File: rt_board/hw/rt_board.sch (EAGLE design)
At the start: 23 parts, among them IC1 MCP170333MB, IC2 FT232RL, Q1 8MHz, U1 STM32F051R8T7, X1 PWR, X2 MINI-USB

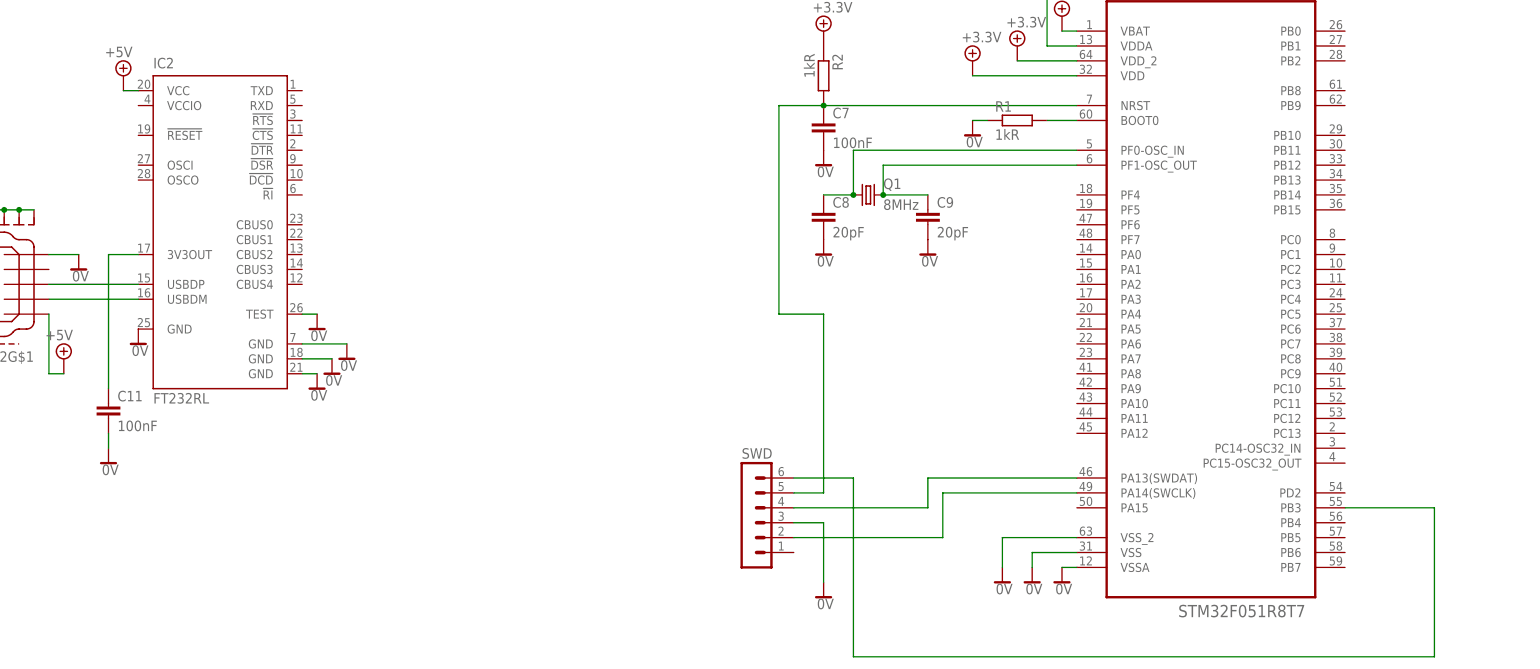
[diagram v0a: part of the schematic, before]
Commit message: fixed SWD connection; added power VccIo to FT232
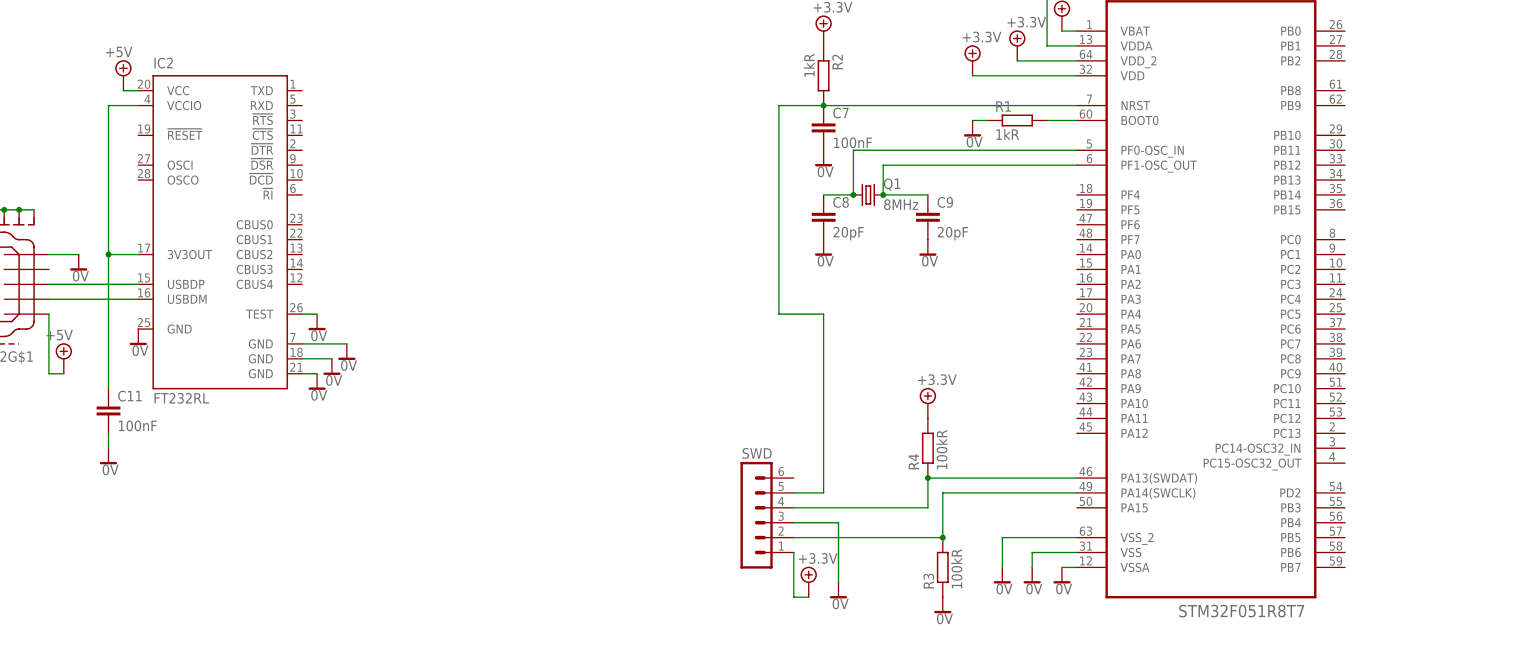
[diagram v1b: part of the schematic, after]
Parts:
- added R3, R4: 100kR, rcl:R-EU_R0603
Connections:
- removed net N$10: SWD.6, U1.PB3
- net +5V: now also R4.2, SWD.1
- net 0V: now also R3.1
- net N$13: now also IC2.VCCIO
- net N$4: now also R3.2
- net N$9: now also R4.1
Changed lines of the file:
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@@
 <part name="C11" library="rcl" deviceset="C-EU" device="C1206" value="100nF"/>
 <part name="SUPPLY33" library="supply2" deviceset="0V" device=""/>
+<part name="SUPPLY34" library="supply2" deviceset="+5V" device="" value="+3.3V"/>
+<part name="R3" library="rcl" deviceset="R-EU_" device="R0603" value="100kR"/>
+<part name="SUPPLY35" library="supply2" deviceset="0V" device=""/>
+<part name="R4" library="rcl" deviceset="R-EU_" device="R0603" value="100kR"/>
+<part name="SUPPLY36" library="supply2" deviceset="+5V" device="" value="+3.3V"/>
 </parts>
 <sheets>
@@
 <instance part="SUPPLY22" gate="0V" x="-40.64" y="93.98"/>
 <instance part="SWD" gate="1" x="-81.28" y="5.08"/>
-<instance part="SUPPLY23" gate="0V" x="-68.58" y="-10.16"/>
+<instance part="SUPPLY23" gate="0V" x="-66.04" y="-10.16"/>
 <instance part="X2" gate="G$1" x="-205.74" y="43.18" rot="R180"/>
 <instance part="X2" gate="S" x="-205.74" y="53.34" rot="R180"/>
@@
 <instance part="C11" gate="G$1" x="-190.5" y="22.86"/>
 <instance part="SUPPLY33" gate="0V" x="-190.5" y="12.7"/>
+<instance part="SUPPLY34" gate="+5V" x="-71.12" y="-7.62"/>
+<instance part="R3" gate="G$1" x="-48.26" y="-5.08" rot="R90"/>
+<instance part="SUPPLY35" gate="0V" x="-48.26" y="-12.7"/>
+<instance part="R4" gate="G$1" x="-50.8" y="15.24" rot="R90"/>
+<instance part="SUPPLY36" gate="+5V" x="-50.8" y="22.86"/>
 </instances>
 <busses>
@@
 <pinref part="SWD" gate="1" pin="3"/>
 <pinref part="SUPPLY23" gate="0V" pin="0V"/>
-<wire x1="-68.58" y1="-7.62" x2="-68.58" y2="2.54" width="0.1524" layer="91"/>
-<wire x1="-68.58" y1="2.54" x2="-73.66" y2="2.54" width="0.1524" layer="91"/>
+<wire x1="-66.04" y1="-7.62" x2="-66.04" y2="2.54" width="0.1524" layer="91"/>
+<wire x1="-66.04" y1="2.54" x2="-73.66" y2="2.54" width="0.1524" layer="91"/>
 </segment>
 <segment>
@@
 <wire x1="-190.5" y1="15.24" x2="-190.5" y2="17.78" width="0.1524" layer="91"/>
 </segment>
+<segment>
+<pinref part="R3" gate="G$1" pin="1"/>
+<pinref part="SUPPLY35" gate="0V" pin="0V"/>
+</segment>
 </net>
 <net name="+5V" class="0">
@@
 <pinref part="SUPPLY19" gate="+5V" pin="+5V"/>
 <wire x1="-60.96" y1="106.68" x2="-58.42" y2="106.68" width="0.1524" layer="91"/>
+</segment>
+<segment>
+<pinref part="SWD" gate="1" pin="1"/>
+<pinref part="SUPPLY34" gate="+5V" pin="+5V"/>
+<wire x1="-71.12" y1="-10.16" x2="-73.66" y2="-10.16" width="0.1524" layer="91"/>
+<wire x1="-73.66" y1="-10.16" x2="-73.66" y2="-2.54" width="0.1524" layer="91"/>
+</segment>
+<segment>
+<pinref part="R4" gate="G$1" pin="2"/>
+<pinref part="SUPPLY36" gate="+5V" pin="+5V"/>
 </segment>
 </net>
@@
 <pinref part="U1" gate="A" pin="PA14(SWCLK)"/>
 <wire x1="-48.26" y1="7.62" x2="-25.4" y2="7.62" width="0.1524" layer="91"/>
+<pinref part="R3" gate="G$1" pin="2"/>
+<junction x="-48.26" y="0"/>
 </segment>
 </net>
@@
 <pinref part="SWD" gate="1" pin="4"/>
 <wire x1="-50.8" y1="5.08" x2="-73.66" y2="5.08" width="0.1524" layer="91"/>
-</segment>
-</net>
-<net name="N$10" class="0">
-<segment>
-<pinref part="U1" gate="A" pin="PB3"/>
-<wire x1="20.32" y1="5.08" x2="35.56" y2="5.08" width="0.1524" layer="91"/>
-<wire x1="35.56" y1="5.08" x2="35.56" y2="-20.32" width="0.1524" layer="91"/>
-<wire x1="35.56" y1="-20.32" x2="-63.5" y2="-20.32" width="0.1524" layer="91"/>
-<wire x1="-63.5" y1="-20.32" x2="-63.5" y2="10.16" width="0.1524" layer="91"/>
-<pinref part="SWD" gate="1" pin="6"/>
-<wire x1="-63.5" y1="10.16" x2="-73.66" y2="10.16" width="0.1524" layer="91"/>
+<pinref part="R4" gate="G$1" pin="1"/>
+<junction x="-50.8" y="10.16"/>
 </segment>
 </net>
@@
 <wire x1="-185.42" y1="48.26" x2="-190.5" y2="48.26" width="0.1524" layer="91"/>
 <wire x1="-190.5" y1="48.26" x2="-190.5" y2="25.4" width="0.1524" layer="91"/>
-</segment>
-</net>
+<pinref part="IC2" gate="1" pin="VCCIO"/>
+<wire x1="-185.42" y1="73.66" x2="-190.5" y2="73.66" width="0.1524" layer="91"/>
+<wire x1="-190.5" y1="73.66" x2="-190.5" y2="48.26" width="0.1524" layer="91"/>
+<junction x="-190.5" y="48.26"/>
+</segment>
+</net>

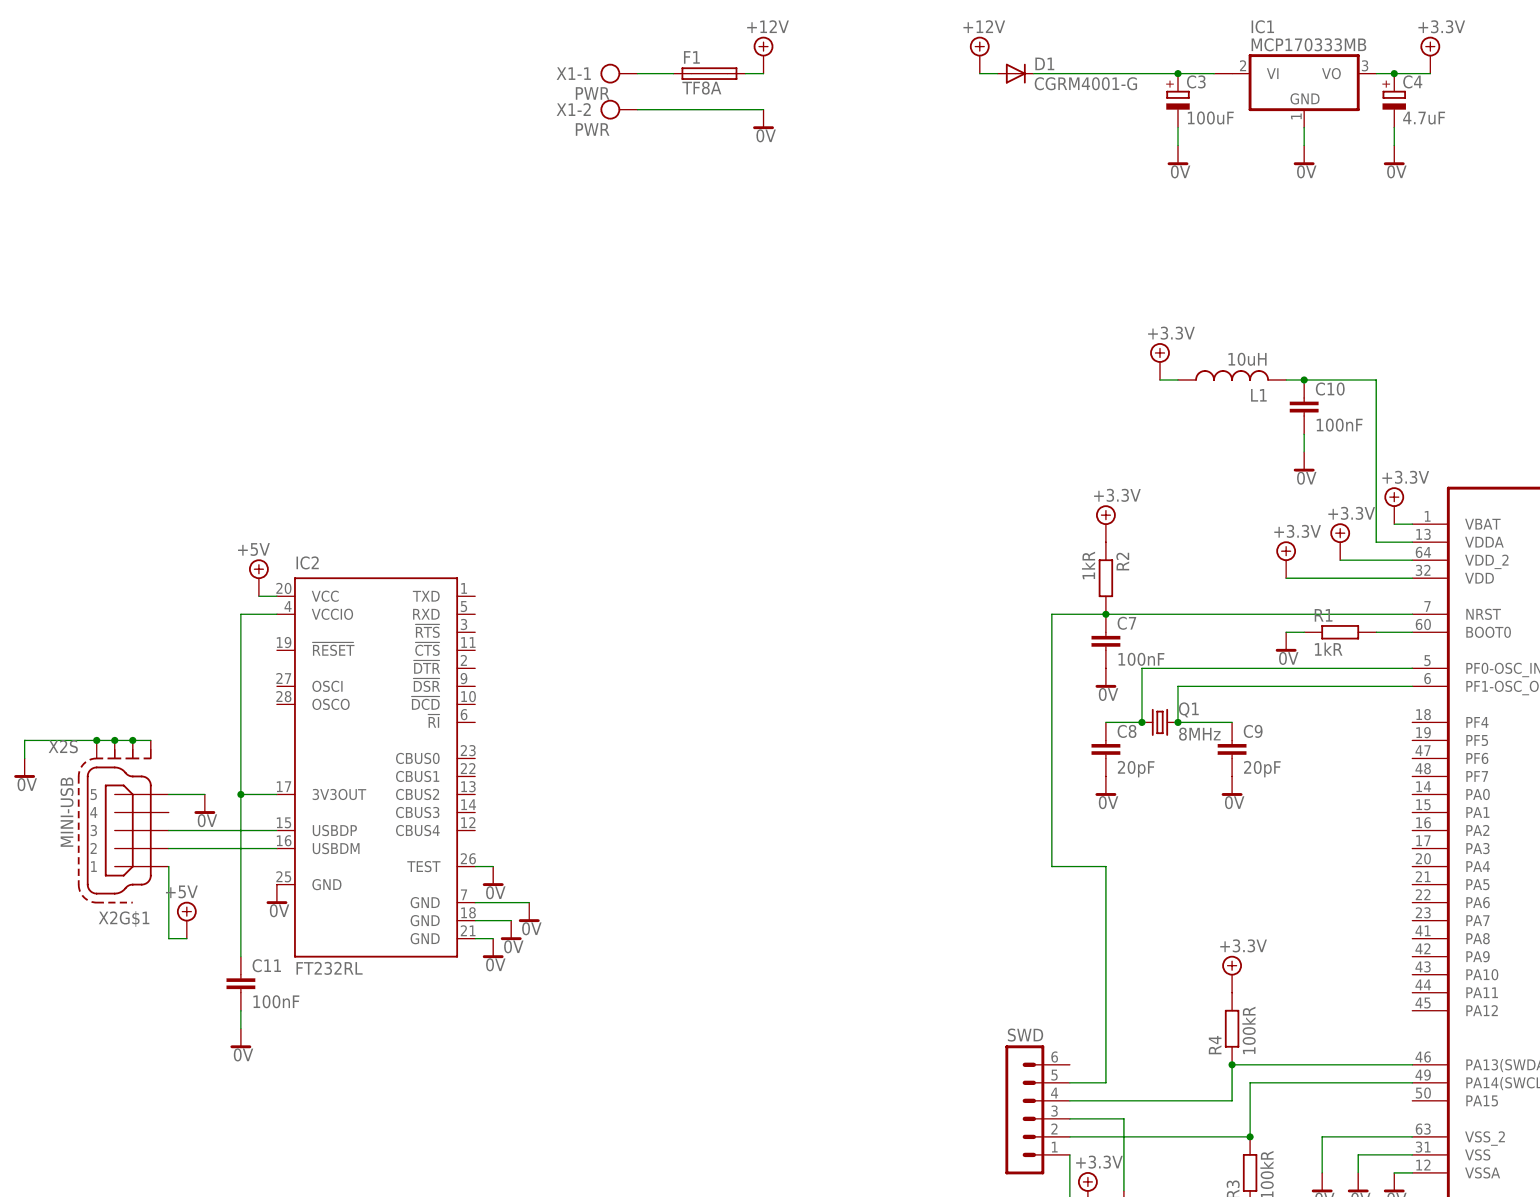
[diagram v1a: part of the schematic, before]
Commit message: resigned from ft232 and USB communication in favor of direct communication with Panda's usart, via sn74avc4t245pw level converter
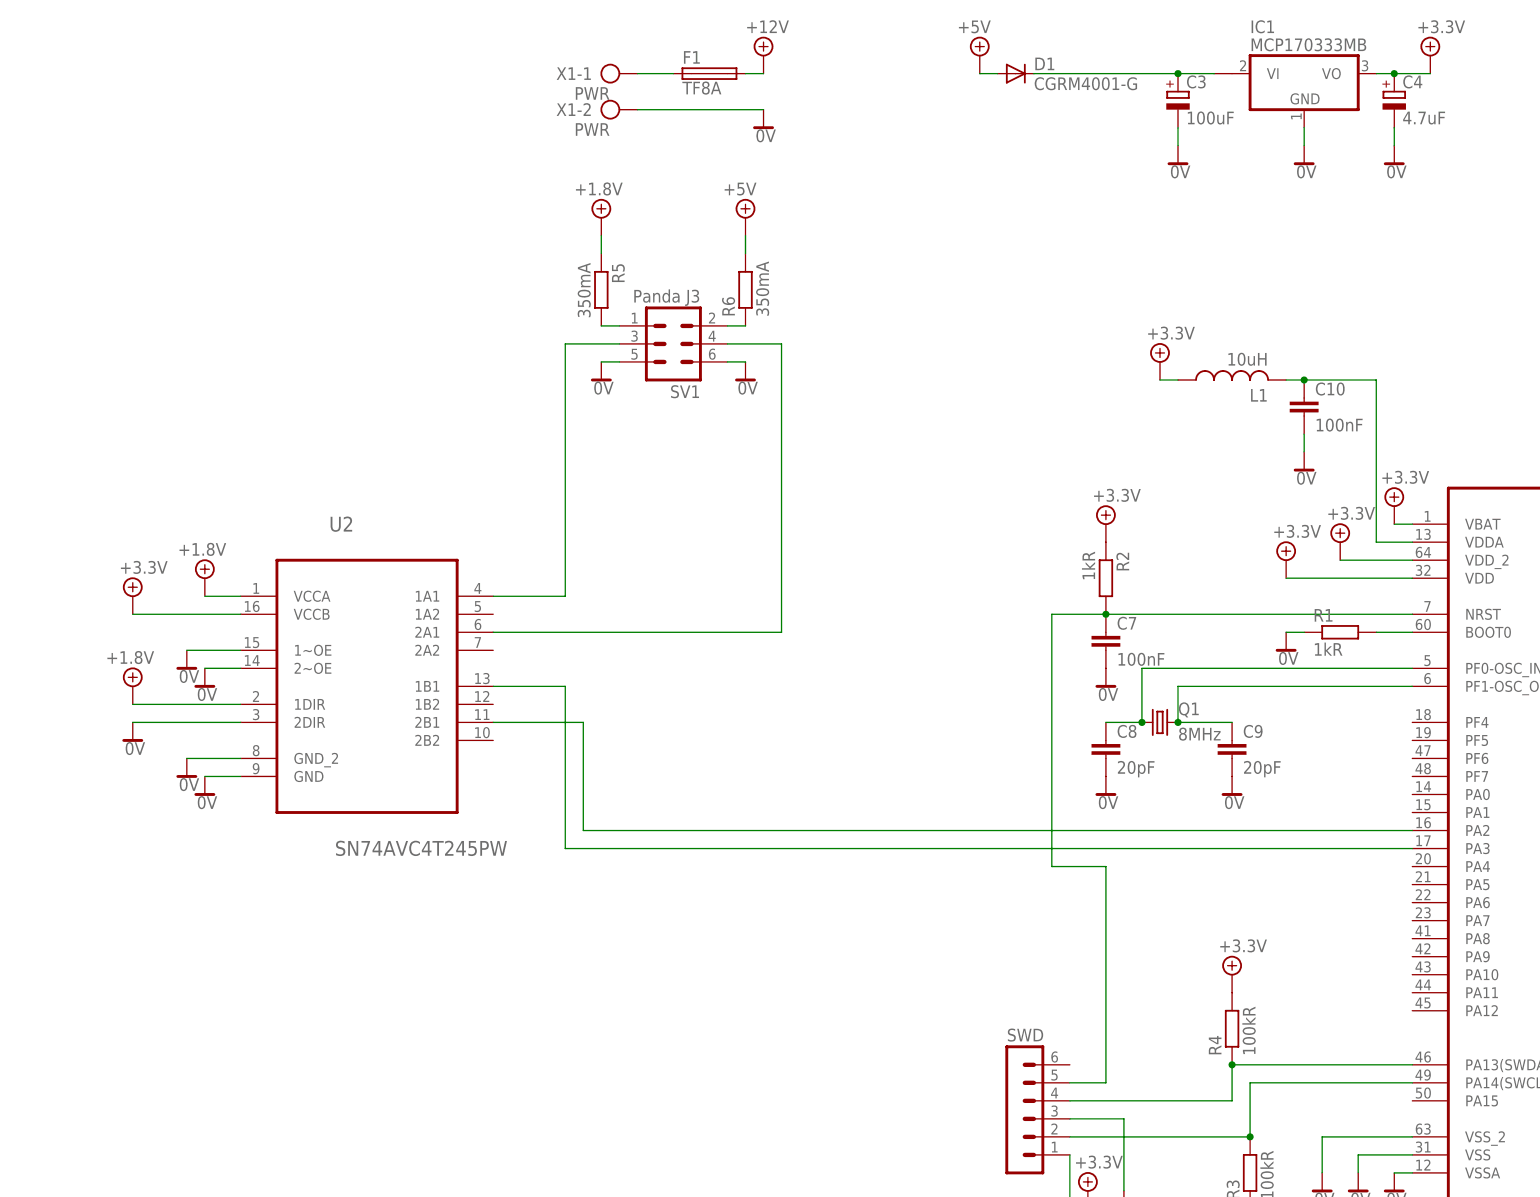
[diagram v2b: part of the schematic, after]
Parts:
- removed C11: 100nF, rcl:C-EUC1206
- removed IC2: FT232RL, ftdichip:FT232RL
- removed X2: MINI-USB, con-cypressindustries:MINI-USB-SCHIELD-32005-201
- added R5, R6: 350mA, rcl:R-EU_MELF0204W
- added SV1: Panda J3, con-lstb:MA03-2
- added U2: SN74AVC4T245PW, TI-SN74AVC4T245PW:SN74AVC4T245PW
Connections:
- new net +5V/4: R5.1, U2.1DIR, U2.VCCA
- new net N$10: R6.1, SV1.2
- new net N$14: U1.PA2, U2.2B1
- new net N$15: SV1.4, U2.2A1
- net +12V: no longer D1.A
- net +5V: now also U2.VCCB
- net +5V/1: now also D1.A, R6.2; no longer IC2.VCC, X2G$1.1
- net 0V: now also SV1.5, SV1.6, U2.1~OE, U2.2DIR, U2.2~OE, U2.GND, U2.GND_2; no longer C11.2, IC2.GND, IC2.GND@1, IC2.GND@2, IC2.GND@A, IC2.TEST, X2G$1.5, X2S.S1, X2S.S2, X2S.S3, X2S.S4
- net N$11: now also R5.2, SV1.1; no longer IC2.USBDM, X2G$1.2
- net N$12: now also SV1.3, U2.1A1; no longer IC2.USBDP, X2G$1.3
- net N$13: now also U1.PA3, U2.1B1; no longer C11.1, IC2.3V3OUT, IC2.VCCIO

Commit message: added power outputs and current control circutyr
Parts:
- added C11, C13, C15, C16, C17, C19, C21, C22: 100nF, rcl:C-EUC1206
- added C12, C18: 100uF, rcl:CPOL-EU153CLV-0810
- added C14, C20: 1nF, rcl:C-EUC1206
- added D2, D3: BZX84CSMD, diode:BZX84CSMD
- added IC2/L1, IC3/L2, IC4/L1, IC5/L2: TLE4935L, allegro:A1202UA
- added R10, R13, R15, R8: 3kR, rcl:R-EU_R0603
- added R11, R16: 3.3kR, rcl:R-EU_R0603
- added R12, R14, R7, R9: 2kR, rcl:R-EU_R0603
- added U3, U5: DRV8801PWP, TI-DRV8801PWP:DRV8801PWP
- added U4, U6: ACS712ELCTR-20A-T, Allegro-ACS712ELCTR-20A-T:ACS712ELCTR-20A-T
- added X2: LEFT, con-ptr500:AK550/2
- added X3: RIGHT, con-ptr500:AK550/2
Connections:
- new net N$16: IC2/L1.OUT, R7.1
- new net N$17: R7.2, R8.1, U1.PA0
- new net N$18: IC3/L2.OUT, R9.1
- new net N$19: R10.1, R9.2, U1.PA1
- new net N$20: U3.OUT+, X2-1.KL
- new net N$21: U3.OUT-, X2-2.KL
- new net N$22: U3.SENSE, U4.IP+, U4.IP+_2
- new net N$23: D2.C, U1.PA4, U4.VIOUT
- new net N$24: C14.1, U4.FILTER
- new net N$25: R11.1, U3.NSLEEP
- new net N$26: C15.2, U3.VCP
- new net N$27: C16.2, U3.CP2
- new net N$28: C16.1, U3.CP1
- new net N$29: IC4/L1.OUT, R12.1
- new net N$30: R12.2, R13.1, U1.PB4
- new net N$31: IC5/L2.OUT, R14.1
- new net N$32: R14.2, R15.1, U1.PB5
- new net N$33: U5.OUT+, X3-1.KL
- new net N$34: U5.OUT-, X3-2.KL
- new net N$35: C20.1, U6.FILTER
- new net N$36: U5.SENSE, U6.IP+, U6.IP+_2
- new net N$37: D3.C, U1.PA5, U6.VIOUT
- new net N$38: R16.1, U5.NSLEEP
- new net N$39: C21.2, U5.VCP
- new net N$40: C22.2, U5.CP2
- new net N$41: C22.1, U5.CP1
- new net N$42: U1.PB13, U3.MODE_1, U5.MODE_1
- new net N$45: U1.PB14, U3.ENABLE
- new net N$46: U1.PB15, U5.ENABLE
- new net N$48: U1.PB12, U3.PHASE
- new net N$49: U1.PB11, U5.PHASE
- net +12V: now also C11.1, C12.+, C15.1, C17.1, C18.+, C21.1, U3.VBB, U5.VBB
- net +5V/1: now also C13.1, C19.1, IC2/L1.VCC, IC3/L2.VCC, IC4/L1.VCC, IC5/L2.VCC, U4.VCC, U6.VCC
- net +5V/4: now also R11.2, R16.2
- net 0V: now also C11.2, C12.-, C13.2, C14.2, C17.2, C18.-, C19.2, C20.2, D2.A, D3.A, IC2/L1.GND, IC3/L2.GND, IC4/L1.GND, IC5/L2.GND, R10.2, R13.2, R15.2, R8.2, U3.EP, U3.GND, U3.GND_2, U3.MODE_2, U4.GND, U4.IP-, U4.IP-_2, U5.EP, U5.GND, U5.GND_2, U5.MODE_2, U6.GND, U6.IP-, U6.IP-_2
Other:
- moved on the sheet: C7, C8, C9, Q1, R2, SWD
